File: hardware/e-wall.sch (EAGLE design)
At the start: 59 parts, among them IC1 74HCT595D, IC2 74HCT595D, IC3 74HCT595D, Q1 BSS123, Q10 BSS123, Q11 BSS123, Q12 BSS123, Q13 BSS123, Q14 BSS123, Q15 BSS123, Q16 BSS123, Q17 BSS123, Q18 BSS123, Q19 BSS123, Q2 BSS123, Q20 BSS123, Q21 BSS123, Q22 BSS123, Q23 BSS123, Q24 BSS123, Q3 BSS123, Q4 BSS123, Q5 BSS123, Q6 BSS123, Q7 BSS123, Q8 BSS123, Q9 BSS123

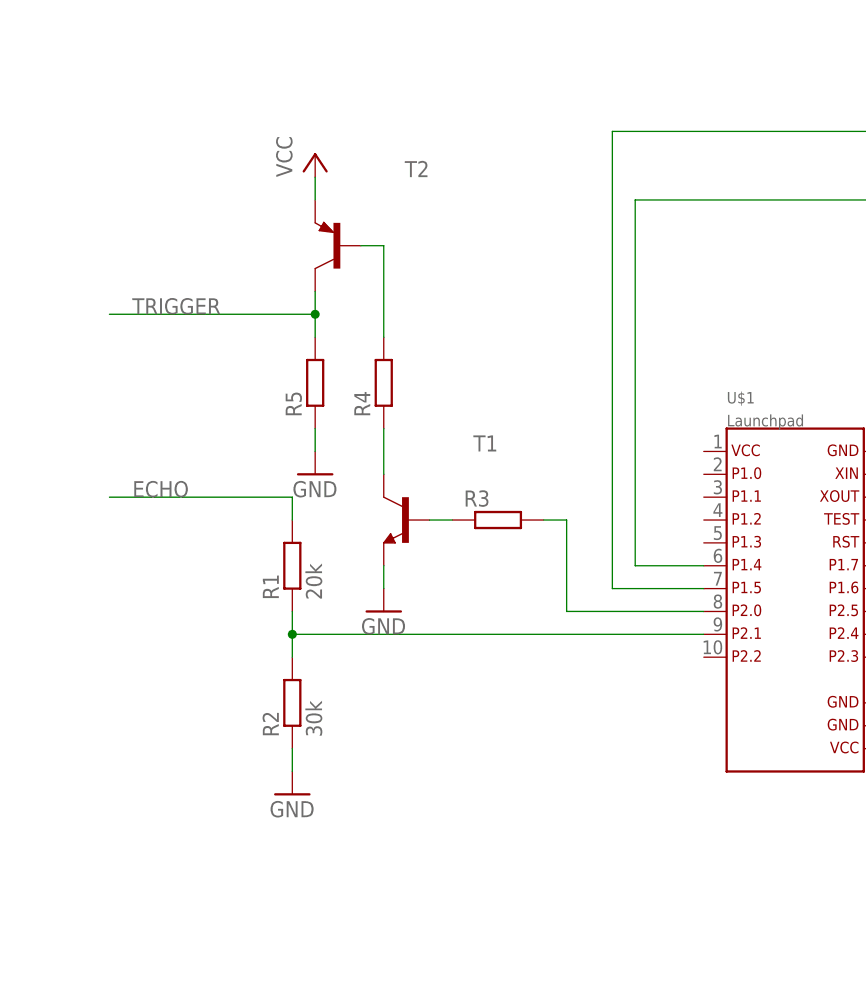
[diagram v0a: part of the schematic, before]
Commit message: Pegelwandler für Trigger korrigiert
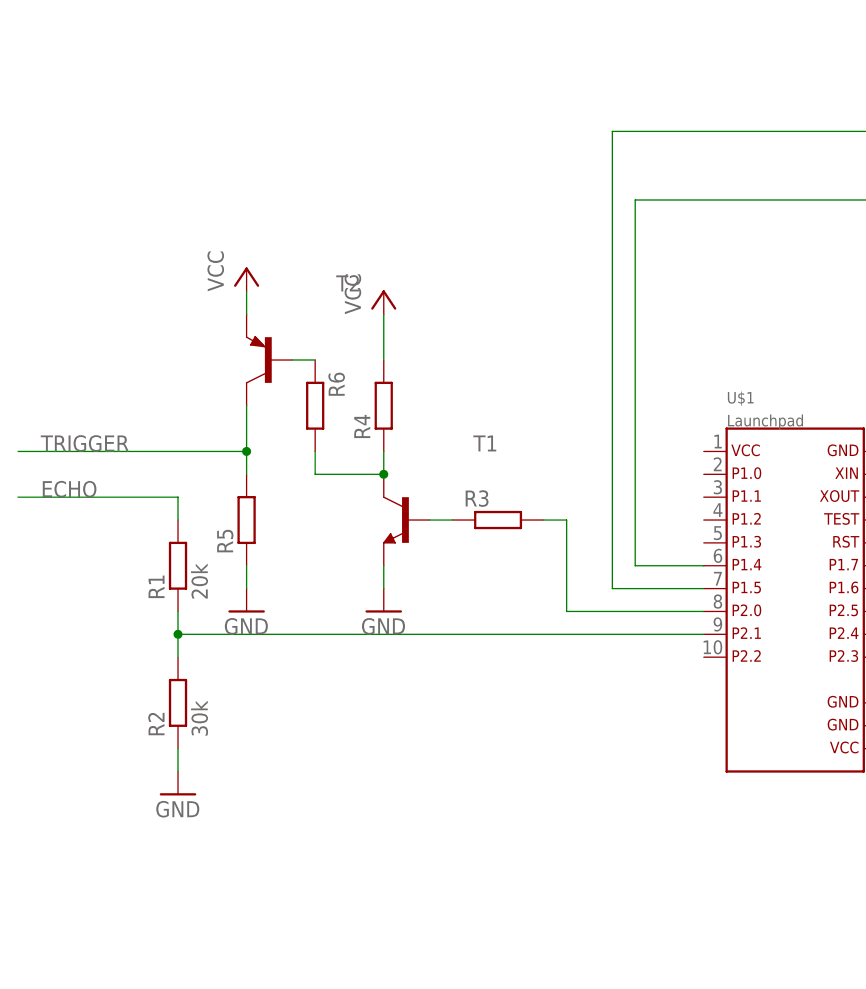
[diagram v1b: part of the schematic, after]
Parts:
- added R6: (no value), resistor:R-EU_R0805
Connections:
- net N$34: now also R6.2
- net N$35: now also R6.1; no longer R4.2
- net VCC: now also R4.2
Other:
- moved on the sheet: R1, R2, R4, R5, T2
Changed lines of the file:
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@@
 <part name="R5" library="resistor" deviceset="R-EU_" device="R0805"/>
 <part name="GND30" library="supply1" deviceset="GND" device=""/>
+<part name="P+29" library="supply1" deviceset="VCC" device=""/>
+<part name="R6" library="resistor" deviceset="R-EU_" device="R0805"/>
 </parts>
 <sheets>
@@
 <instance part="P+26" gate="1" x="447.04" y="68.58"/>
 <instance part="P+27" gate="1" x="447.04" y="43.18"/>
-<instance part="R1" gate="G$1" x="22.86" y="60.96" rot="R90"/>
-<instance part="R2" gate="G$1" x="22.86" y="45.72" rot="R90"/>
+<instance part="R1" gate="G$1" x="10.16" y="60.96" rot="R90"/>
+<instance part="R2" gate="G$1" x="10.16" y="45.72" rot="R90"/>
 <instance part="R3" gate="G$1" x="45.72" y="66.04"/>
-<instance part="R4" gate="G$1" x="33.02" y="81.28" rot="R90"/>
+<instance part="R4" gate="G$1" x="33.02" y="78.74" rot="R90"/>
 <instance part="T1" gate="G$1" x="35.56" y="66.04" rot="MR0"/>
 <instance part="GND28" gate="1" x="33.02" y="55.88"/>
-<instance part="GND29" gate="1" x="22.86" y="35.56"/>
-<instance part="P+28" gate="VCC" x="25.4" y="106.68"/>
-<instance part="T2" gate="G$1" x="27.94" y="96.52" rot="MR0"/>
-<instance part="R5" gate="G$1" x="25.4" y="81.28" rot="R90"/>
-<instance part="GND30" gate="1" x="25.4" y="71.12"/>
+<instance part="GND29" gate="1" x="10.16" y="35.56"/>
+<instance part="P+28" gate="VCC" x="17.78" y="93.98"/>
+<instance part="T2" gate="G$1" x="20.32" y="83.82" rot="MR0"/>
+<instance part="R5" gate="G$1" x="17.78" y="66.04" rot="R90"/>
+<instance part="GND30" gate="1" x="17.78" y="55.88"/>
+<instance part="P+29" gate="VCC" x="33.02" y="91.44"/>
+<instance part="R6" gate="G$1" x="25.4" y="78.74" rot="R270"/>
 </instances>
 <busses>
@@
 <pinref part="R2" gate="G$1" pin="1"/>
 <pinref part="GND29" gate="1" pin="GND"/>
-<wire x1="22.86" y1="40.64" x2="22.86" y2="38.1" width="0.1524" layer="91"/>
+<wire x1="10.16" y1="40.64" x2="10.16" y2="38.1" width="0.1524" layer="91"/>
 </segment>
 <segment>
@@
 <pinref part="R5" gate="G$1" pin="1"/>
 <pinref part="GND30" gate="1" pin="GND"/>
-<wire x1="25.4" y1="76.2" x2="25.4" y2="73.66" width="0.1524" layer="91"/>
+<wire x1="17.78" y1="58.42" x2="17.78" y2="60.96" width="0.1524" layer="91"/>
 </segment>
 </net>
@@
 <pinref part="P+28" gate="VCC" pin="VCC"/>
 <pinref part="T2" gate="G$1" pin="E"/>
-<wire x1="25.4" y1="104.14" x2="25.4" y2="101.6" width="0.1524" layer="91"/>
+<wire x1="17.78" y1="91.44" x2="17.78" y2="88.9" width="0.1524" layer="91"/>
+</segment>
+<segment>
+<pinref part="R4" gate="G$1" pin="2"/>
+<pinref part="P+29" gate="VCC" pin="VCC"/>
+<wire x1="33.02" y1="88.9" x2="33.02" y2="83.82" width="0.1524" layer="91"/>
 </segment>
 </net>
@@
 <pinref part="R1" gate="G$1" pin="1"/>
 <pinref part="R2" gate="G$1" pin="2"/>
-<wire x1="22.86" y1="55.88" x2="22.86" y2="53.34" width="0.1524" layer="91"/>
+<wire x1="10.16" y1="55.88" x2="10.16" y2="53.34" width="0.1524" layer="91"/>
 <pinref part="U$1" gate="G$1" pin="9"/>
-<wire x1="22.86" y1="53.34" x2="22.86" y2="50.8" width="0.1524" layer="91"/>
-<wire x1="22.86" y1="53.34" x2="68.58" y2="53.34" width="0.1524" layer="91"/>
-<junction x="22.86" y="53.34"/>
+<wire x1="10.16" y1="53.34" x2="10.16" y2="50.8" width="0.1524" layer="91"/>
+<wire x1="10.16" y1="53.34" x2="68.58" y2="53.34" width="0.1524" layer="91"/>
+<junction x="10.16" y="53.34"/>
 </segment>
 </net>
@@
 <segment>
 <pinref part="R1" gate="G$1" pin="2"/>
-<wire x1="22.86" y1="66.04" x2="22.86" y2="68.58" width="0.1524" layer="91"/>
-<wire x1="22.86" y1="68.58" x2="2.54" y2="68.58" width="0.1524" layer="91"/>
-<label x="5.08" y="68.58" size="1.778" layer="95"/>
+<wire x1="10.16" y1="66.04" x2="10.16" y2="68.58" width="0.1524" layer="91"/>
+<wire x1="10.16" y1="68.58" x2="-7.62" y2="68.58" width="0.1524" layer="91"/>
+<label x="-5.08" y="68.58" size="1.778" layer="95"/>
 </segment>
 </net>
@@
 <pinref part="R4" gate="G$1" pin="1"/>
 <pinref part="T1" gate="G$1" pin="C"/>
-<wire x1="33.02" y1="76.2" x2="33.02" y2="71.12" width="0.1524" layer="91"/>
-</segment>
-</net>
-<net name="N$35" class="0">
-<segment>
-<pinref part="T2" gate="G$1" pin="B"/>
-<pinref part="R4" gate="G$1" pin="2"/>
-<wire x1="30.48" y1="96.52" x2="33.02" y2="96.52" width="0.1524" layer="91"/>
-<wire x1="33.02" y1="96.52" x2="33.02" y2="86.36" width="0.1524" layer="91"/>
+<wire x1="33.02" y1="73.66" x2="33.02" y2="71.12" width="0.1524" layer="91"/>
+<pinref part="R6" gate="G$1" pin="2"/>
+<wire x1="25.4" y1="73.66" x2="25.4" y2="71.12" width="0.1524" layer="91"/>
+<wire x1="25.4" y1="71.12" x2="33.02" y2="71.12" width="0.1524" layer="91"/>
+<junction x="33.02" y="71.12"/>
 </segment>
 </net>
@@
 <pinref part="T2" gate="G$1" pin="C"/>
 <pinref part="R5" gate="G$1" pin="2"/>
-<wire x1="25.4" y1="91.44" x2="25.4" y2="88.9" width="0.1524" layer="91"/>
-<wire x1="25.4" y1="88.9" x2="25.4" y2="86.36" width="0.1524" layer="91"/>
-<wire x1="25.4" y1="88.9" x2="2.54" y2="88.9" width="0.1524" layer="91"/>
-<junction x="25.4" y="88.9"/>
-<label x="5.08" y="88.9" size="1.778" layer="95"/>
-</segment>
-</net>
+<wire x1="17.78" y1="78.74" x2="17.78" y2="73.66" width="0.1524" layer="91"/>
+<wire x1="17.78" y1="73.66" x2="17.78" y2="71.12" width="0.1524" layer="91"/>
+<wire x1="17.78" y1="73.66" x2="-7.62" y2="73.66" width="0.1524" layer="91"/>
+<junction x="17.78" y="73.66"/>
+<label x="-5.08" y="73.66" size="1.778" layer="95"/>
+</segment>
+</net>
+<net name="N$35" class="0">
+<segment>
+<pinref part="T2" gate="G$1" pin="B"/>
+<pinref part="R6" gate="G$1" pin="1"/>
+<wire x1="22.86" y1="83.82" x2="25.4" y2="83.82" width="0.1524" layer="91"/>
+</segment>
+</net>

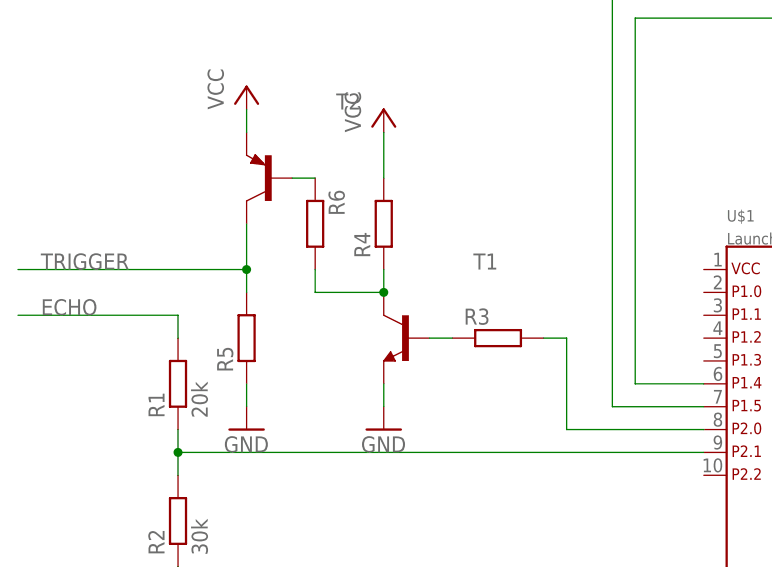
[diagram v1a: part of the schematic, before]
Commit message: Bauteilwerte Pegelwandler Trigger
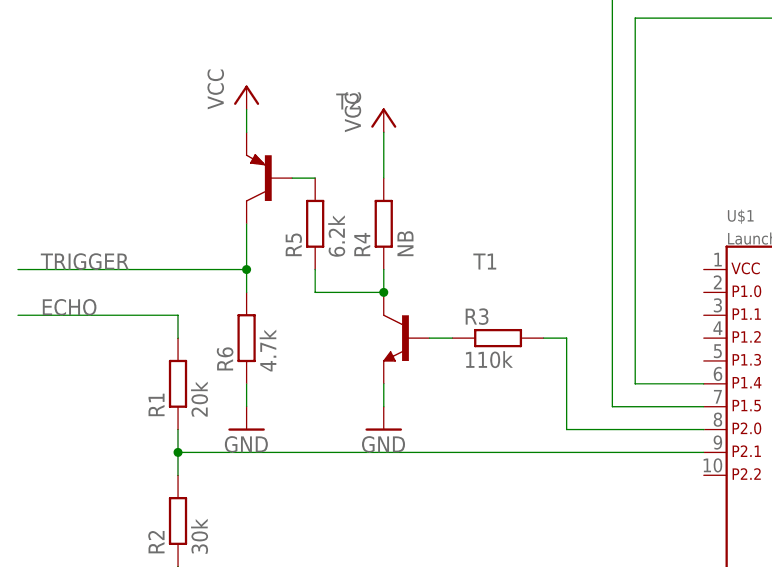
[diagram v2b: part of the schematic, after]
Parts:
- R3: value (none) -> 110k
- R4: value (none) -> NB
- R5: value (none) -> 6.2k
- R6: value (none) -> 4.7k
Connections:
- net GND: now also R6.1; no longer R5.1
- net N$34: now also R5.1; no longer R6.2
- net N$35: now also R5.2; no longer R6.1
- net TRIGGER: now also R6.2; no longer R5.2
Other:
- moved on the sheet: R5, R6
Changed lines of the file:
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@@
 <part name="R1" library="resistor" deviceset="R-EU_" device="R0805" value="20k"/>
 <part name="R2" library="resistor" deviceset="R-EU_" device="R0805" value="30k"/>
-<part name="R3" library="resistor" deviceset="R-EU_" device="R0805"/>
-<part name="R4" library="resistor" deviceset="R-EU_" device="R0805"/>
+<part name="R3" library="resistor" deviceset="R-EU_" device="R0805" value="110k"/>
+<part name="R4" library="resistor" deviceset="R-EU_" device="R0805" value="NB"/>
 <part name="T1" library="transistor" deviceset="*-NPN-" device="SOT23-EBC"/>
 <part name="GND28" library="supply1" deviceset="GND" device=""/>
@@
 <part name="P+28" library="supply1" deviceset="VCC" device=""/>
 <part name="T2" library="transistor" deviceset="*-PNP-" device="SOT23-EBC"/>
-<part name="R5" library="resistor" deviceset="R-EU_" device="R0805"/>
+<part name="R6" library="resistor" deviceset="R-EU_" device="R0805" value="4.7k"/>
 <part name="GND30" library="supply1" deviceset="GND" device=""/>
 <part name="P+29" library="supply1" deviceset="VCC" device=""/>
-<part name="R6" library="resistor" deviceset="R-EU_" device="R0805"/>
+<part name="R5" library="resistor" deviceset="R-EU_" device="R0805" value="6.2k"/>
 </parts>
 <sheets>
@@
 <instance part="P+28" gate="VCC" x="17.78" y="93.98"/>
 <instance part="T2" gate="G$1" x="20.32" y="83.82" rot="MR0"/>
-<instance part="R5" gate="G$1" x="17.78" y="66.04" rot="R90"/>
+<instance part="R6" gate="G$1" x="17.78" y="66.04" rot="R90"/>
 <instance part="GND30" gate="1" x="17.78" y="55.88"/>
 <instance part="P+29" gate="VCC" x="33.02" y="91.44"/>
-<instance part="R6" gate="G$1" x="25.4" y="78.74" rot="R270"/>
+<instance part="R5" gate="G$1" x="25.4" y="78.74" rot="R90"/>
 </instances>
 <busses>
@@
 </segment>
 <segment>
-<pinref part="R5" gate="G$1" pin="1"/>
+<pinref part="R6" gate="G$1" pin="1"/>
 <pinref part="GND30" gate="1" pin="GND"/>
 <wire x1="17.78" y1="58.42" x2="17.78" y2="60.96" width="0.1524" layer="91"/>
@@
 <pinref part="T1" gate="G$1" pin="C"/>
 <wire x1="33.02" y1="73.66" x2="33.02" y2="71.12" width="0.1524" layer="91"/>
-<pinref part="R6" gate="G$1" pin="2"/>
-<wire x1="25.4" y1="73.66" x2="25.4" y2="71.12" width="0.1524" layer="91"/>
 <wire x1="25.4" y1="71.12" x2="33.02" y2="71.12" width="0.1524" layer="91"/>
 <junction x="33.02" y="71.12"/>
+<pinref part="R5" gate="G$1" pin="1"/>
+<wire x1="25.4" y1="73.66" x2="25.4" y2="71.12" width="0.1524" layer="91"/>
 </segment>
 </net>
@@
 <segment>
 <pinref part="T2" gate="G$1" pin="C"/>
-<pinref part="R5" gate="G$1" pin="2"/>
+<pinref part="R6" gate="G$1" pin="2"/>
 <wire x1="17.78" y1="78.74" x2="17.78" y2="73.66" width="0.1524" layer="91"/>
 <wire x1="17.78" y1="73.66" x2="17.78" y2="71.12" width="0.1524" layer="91"/>
@@
 <segment>
 <pinref part="T2" gate="G$1" pin="B"/>
-<pinref part="R6" gate="G$1" pin="1"/>
+<pinref part="R5" gate="G$1" pin="2"/>
 <wire x1="22.86" y1="83.82" x2="25.4" y2="83.82" width="0.1524" layer="91"/>
 </segment>

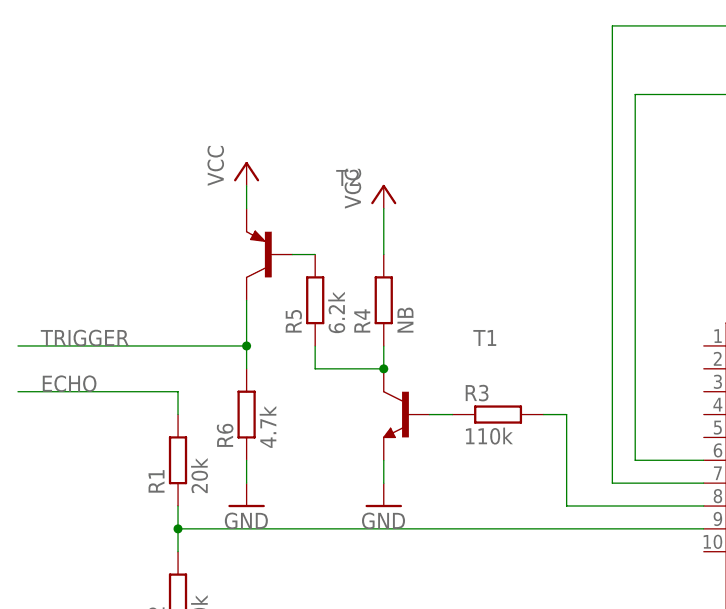
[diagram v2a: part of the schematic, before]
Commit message: Transistoren beschriftet
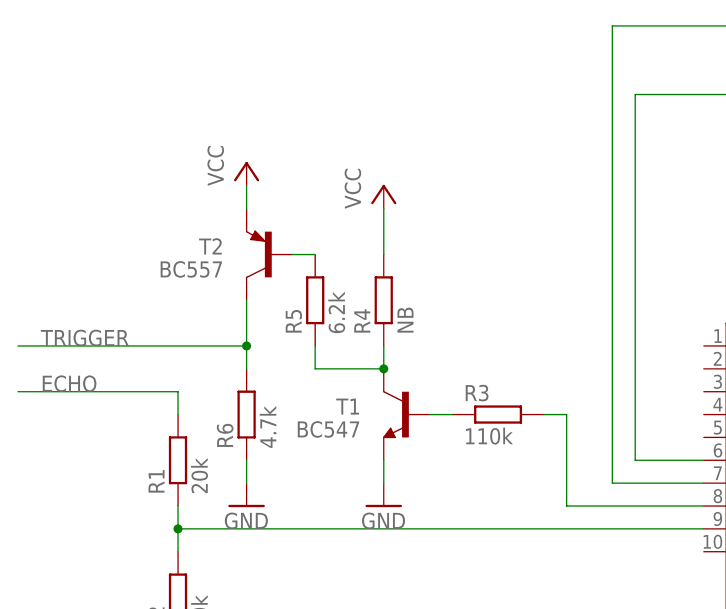
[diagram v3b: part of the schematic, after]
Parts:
- T1: value (none) -> BC547
- T2: value (none) -> BC557
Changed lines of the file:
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@@
 <part name="R3" library="resistor" deviceset="R-EU_" device="R0805" value="110k"/>
 <part name="R4" library="resistor" deviceset="R-EU_" device="R0805" value="NB"/>
-<part name="T1" library="transistor" deviceset="*-NPN-" device="SOT23-EBC"/>
+<part name="T1" library="transistor" deviceset="*-NPN-" device="SOT23-EBC" value="BC547"/>
 <part name="GND28" library="supply1" deviceset="GND" device=""/>
 <part name="GND29" library="supply1" deviceset="GND" device=""/>
 <part name="P+28" library="supply1" deviceset="VCC" device=""/>
-<part name="T2" library="transistor" deviceset="*-PNP-" device="SOT23-EBC"/>
+<part name="T2" library="transistor" deviceset="*-PNP-" device="SOT23-EBC" value="BC557"/>
 <part name="R6" library="resistor" deviceset="R-EU_" device="R0805" value="4.7k"/>
 <part name="GND30" library="supply1" deviceset="GND" device=""/>
@@
 <instance part="R3" gate="G$1" x="45.72" y="66.04"/>
 <instance part="R4" gate="G$1" x="33.02" y="78.74" rot="R90"/>
-<instance part="T1" gate="G$1" x="35.56" y="66.04" rot="MR0"/>
+<instance part="T1" gate="G$1" x="35.56" y="66.04" smashed="yes" rot="MR0">
+<attribute name="NAME" x="30.48" y="66.04" size="1.778" layer="95" rot="MR0"/>
+<attribute name="VALUE" x="30.48" y="63.5" size="1.778" layer="96" rot="MR0"/>
+</instance>
 <instance part="GND28" gate="1" x="33.02" y="55.88"/>
 <instance part="GND29" gate="1" x="10.16" y="35.56"/>
 <instance part="P+28" gate="VCC" x="17.78" y="93.98"/>
-<instance part="T2" gate="G$1" x="20.32" y="83.82" rot="MR0"/>
+<instance part="T2" gate="G$1" x="20.32" y="83.82" smashed="yes" rot="MR0">
+<attribute name="NAME" x="15.24" y="83.82" size="1.778" layer="95" rot="MR0"/>
+<attribute name="VALUE" x="15.24" y="81.28" size="1.778" layer="96" rot="MR0"/>
+</instance>
 <instance part="R6" gate="G$1" x="17.78" y="66.04" rot="R90"/>
 <instance part="GND30" gate="1" x="17.78" y="55.88"/>

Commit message: Schaltung Netzteileinschaltung
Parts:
- added R7: 7.5k, resistor:R-EU_R0805
- added T3: BC547, transistor:-NPN-SOT23-EBC
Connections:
- new net N$36: R7.1, T3.B
- new net N$37: R7.2, U$1.10
- new net POWER_ON: T3.C
- net GND: now also T3.E
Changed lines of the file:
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@@
 <part name="P+29" library="supply1" deviceset="VCC" device=""/>
 <part name="R5" library="resistor" deviceset="R-EU_" device="R0805" value="6.2k"/>
+<part name="T3" library="transistor" deviceset="*-NPN-" device="SOT23-EBC" value="BC547"/>
+<part name="R7" library="resistor" deviceset="R-EU_" device="R0805" value="7.5k"/>
+<part name="GND31" library="supply1" deviceset="GND" device=""/>
 </parts>
 <sheets>
@@
 <instance part="P+29" gate="VCC" x="33.02" y="91.44"/>
 <instance part="R5" gate="G$1" x="25.4" y="78.74" rot="R90"/>
+<instance part="T3" gate="G$1" x="25.4" y="22.86" smashed="yes" rot="MR0">
+<attribute name="NAME" x="20.32" y="22.86" size="1.778" layer="95" rot="MR0"/>
+<attribute name="VALUE" x="20.32" y="20.32" size="1.778" layer="96" rot="MR0"/>
+</instance>
+<instance part="R7" gate="G$1" x="35.56" y="22.86"/>
+<instance part="GND31" gate="1" x="22.86" y="12.7"/>
 </instances>
 <busses>
@@
 <pinref part="GND30" gate="1" pin="GND"/>
 <wire x1="17.78" y1="58.42" x2="17.78" y2="60.96" width="0.1524" layer="91"/>
+</segment>
+<segment>
+<pinref part="T3" gate="G$1" pin="E"/>
+<pinref part="GND31" gate="1" pin="GND"/>
+<wire x1="22.86" y1="17.78" x2="22.86" y2="15.24" width="0.1524" layer="91"/>
 </segment>
 </net>
@@
 </segment>
 </net>
+<net name="N$36" class="0">
+<segment>
+<pinref part="R7" gate="G$1" pin="1"/>
+<pinref part="T3" gate="G$1" pin="B"/>
+<wire x1="30.48" y1="22.86" x2="27.94" y2="22.86" width="0.1524" layer="91"/>
+</segment>
+</net>
+<net name="N$37" class="0">
+<segment>
+<pinref part="R7" gate="G$1" pin="2"/>
+<wire x1="40.64" y1="22.86" x2="45.72" y2="22.86" width="0.1524" layer="91"/>
+<wire x1="45.72" y1="22.86" x2="45.72" y2="50.8" width="0.1524" layer="91"/>
+<pinref part="U$1" gate="G$1" pin="10"/>
+<wire x1="45.72" y1="50.8" x2="68.58" y2="50.8" width="0.1524" layer="91"/>
+</segment>
+</net>
+<net name="POWER_ON" class="0">
+<segment>
+<pinref part="T3" gate="G$1" pin="C"/>
+<wire x1="22.86" y1="27.94" x2="22.86" y2="30.48" width="0.1524" layer="91"/>
+<wire x1="22.86" y1="30.48" x2="-7.62" y2="30.48" width="0.1524" layer="91"/>
+<label x="-5.08" y="30.48" size="1.778" layer="95"/>
+</segment>
+</net>
